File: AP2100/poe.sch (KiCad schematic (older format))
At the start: 53 parts, among them IC1 FDS86242, Q1 HMHA2801AR2, U1 TPS23751PWP, U2 TL431DBV

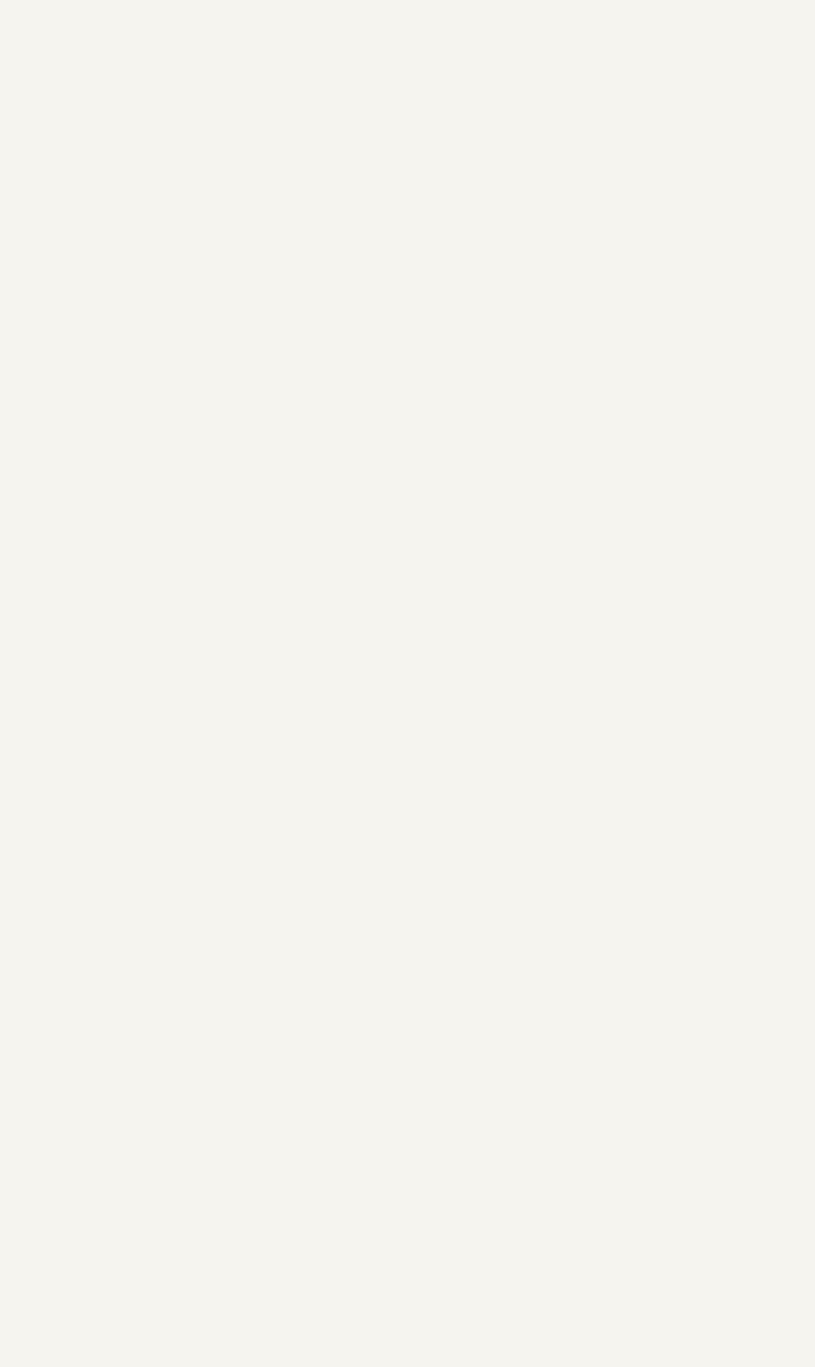
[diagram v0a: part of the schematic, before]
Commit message: Update hydroponics BOM + pdf. Add PM8804/8805 library parts and schematic with them on it
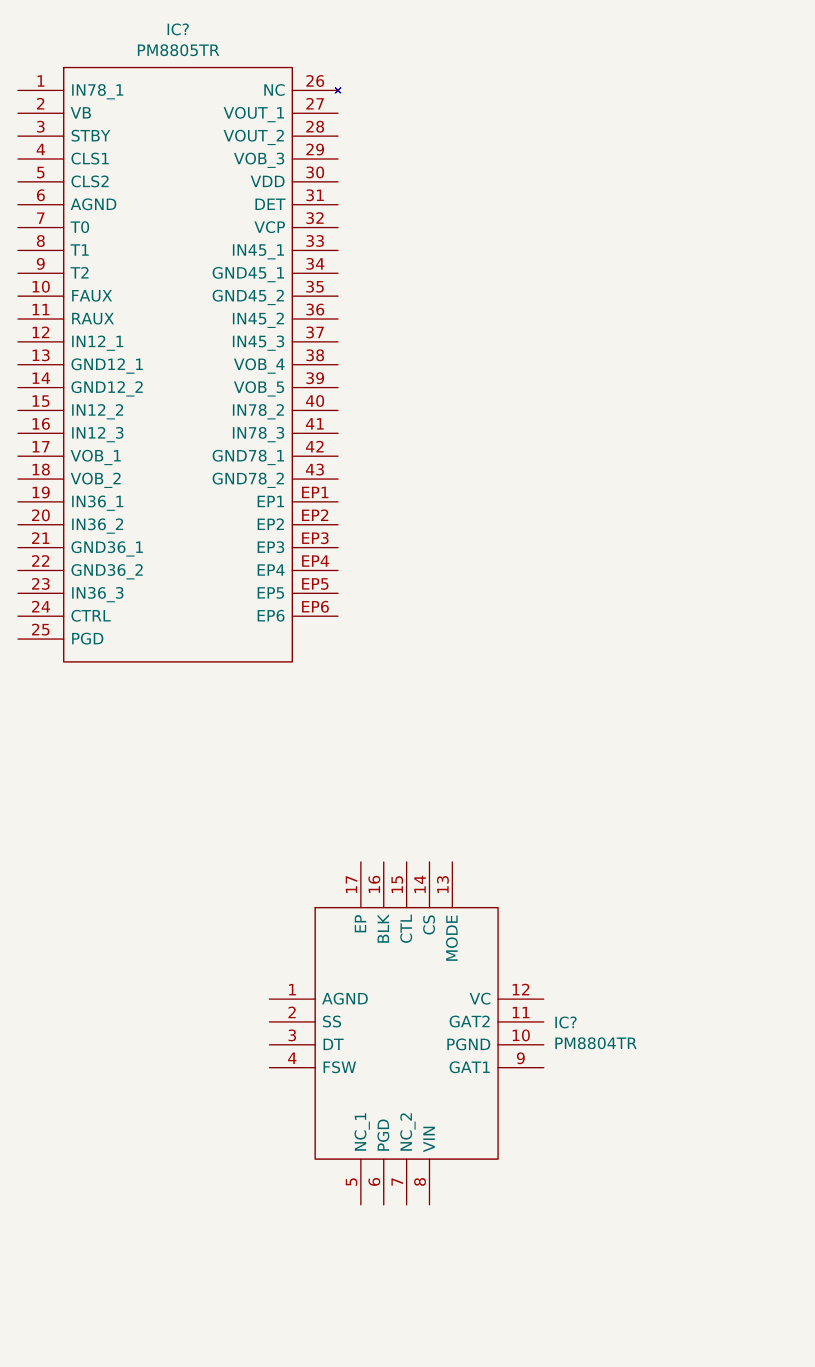
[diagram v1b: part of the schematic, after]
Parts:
- added IC?: PM8805TR, PM8805TR, symbol PM8805TR:PM8805TR
- added IC?: PM8804TR, QFN50P340X340X90-17N, symbol PM8804TR:PM8804TR
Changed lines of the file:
@@
 NoConn ~ 16425 6375
 NoConn ~ 16425 6875
+$Comp
+L PM8805TR:PM8805TR IC?
+U 1 1 5EFD32AF
+P 1950 1550
+F 0 "IC?" H 2650 1815 50  0000 C CNN
+F 1 "PM8805TR" H 2650 1724 50  0000 C CNN
+F 2 "PM8805TR" H 3200 1650 50  0001 L CNN
+F 3 "https://www.st.com/resource/en/datasheet/pm8805.pdf" H 3200 1550 50  0001 L CNN
+F 4 "STMICROELECTRONICS - PM8805TR - POE/PD CONTROLLER, -40 TO 85DEG C" H 3200 1450 50  0001 L CNN "Description"
+F 5 "4" H 3200 1350 50  0001 L CNN "Height"
+F 6 "STMicroelectronics" H 3200 1250 50  0001 L CNN "Manufacturer_Name"
+F 7 "PM8805TR" H 3200 1150 50  0001 L CNN "Manufacturer_Part_Number"
+F 8 "PM8805TR" H 3200 1050 50  0001 L CNN "Arrow Part Number"
+F 9 "https://www.arrow.com/en/products/pm8805tr/stmicroelectronics" H 3200 950 50  0001 L CNN "Arrow Price/Stock"
+F 10 "511-PM8805TR" H 3200 850 50  0001 L CNN "Mouser Part Number"
+F 11 "https://www.mouser.com/Search/Refine.aspx?Keyword=511-PM8805TR" H 3200 750 50  0001 L CNN "Mouser Price/Stock"
+	1    1950 1550
+	1    0    0    -1
+$EndComp
+$Comp
+L PM8804TR:PM8804TR IC?
+U 1 1 5EFD4BD6
+P 3050 5525
+F 0 "IC?" H 4294 5421 50  0000 L CNN
+F 1 "PM8804TR" H 4294 5330 50  0000 L CNN
+F 2 "QFN50P340X340X90-17N" H 4100 5925 50  0001 L CNN
+F 3 "https://www.st.com/resource/en/datasheet/pm8804.pdf" H 4100 5825 50  0001 L CNN
+F 4 "STMicroelectronics PM8804TR PWM Current Mode Controller, Low Side Gate Driver, 10  75V 16-Pin, VFQFPN" H 4100 5725 50  0001 L CNN "Description"
+F 5 "0.9" H 4100 5625 50  0001 L CNN "Height"
+F 6 "STMicroelectronics" H 4100 5525 50  0001 L CNN "Manufacturer_Name"
+F 7 "PM8804TR" H 4100 5425 50  0001 L CNN "Manufacturer_Part_Number"
+F 8 "PM8804TR" H 4100 5325 50  0001 L CNN "Arrow Part Number"
+F 9 "" H 4100 5225 50  0001 L CNN "Arrow Price/Stock"
+F 10 "" H 4100 5125 50  0001 L CNN "Mouser Part Number"
+F 11 "" H 4100 5025 50  0001 L CNN "Mouser Price/Stock"
+	1    3050 5525
+	1    0    0    -1
+$EndComp
 $EndSCHEMATC
